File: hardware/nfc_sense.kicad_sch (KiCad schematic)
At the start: 27 parts, among them U1 TMP112AIDRLT, U2 RF430CL330HIRGTR‎, U3 ATtiny3227-M

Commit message: triangle extension
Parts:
- removed C8: 0.1 yF, Capacitor_SMD:C_0603_1608Metric, symbol Device:C
- removed D3: D_Schottky, Diode_SMD:D_0603_1608Metric_Pad1.05x0.95mm_HandSolder, symbol Device:D_Schottky
- removed R4: 10k, Resistor_SMD:R_0603_1608Metric_Pad0.98x0.95mm_HandSolder, symbol Device:R
- removed TP3, TP5: TestPoint, TestPoint:TestPoint_Pad_D1.0mm, symbol Connector:TestPoint

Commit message: attiny426 revision
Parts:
- removed U3: ATtiny3227-M, Package_DFN_QFN:QFN-24-1EP_4x4mm_P0.5mm_EP2.6x2.6mm, symbol MCU_Microchip_ATtiny:ATtiny3227-M
- added TP4: TestPoint, TestPoint:TestPoint_Pad_D1.0mm, symbol Connector:TestPoint
- added U3: ATtiny426-M, Package_DFN_QFN:VQFN-20-1EP_3x3mm_P0.4mm_EP1.7x1.7mm, symbol MCU_Microchip_ATtiny:ATtiny426-M
- renumbered TP4 to TP3
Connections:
- net ALERT: now also U3.18 (PC3)
- net GND: now also U3.21 (GND), U3.3 (GND)
- net RF430_INT: now also U3.10 (PB4)
- net RF430_RST: now also U3.9 (PB5)
- net RX: now also U3.11 (PB3)
- net SCL: now also U3.14 (PB0)
- net SDA: now also U3.13 (PB1)
- net TX: now also U3.12 (PB2)
- net UPDI: now also U3.19 (~{RESET}/PA0)
- net VCC: now also TP4.1, U3.4 (VCC)

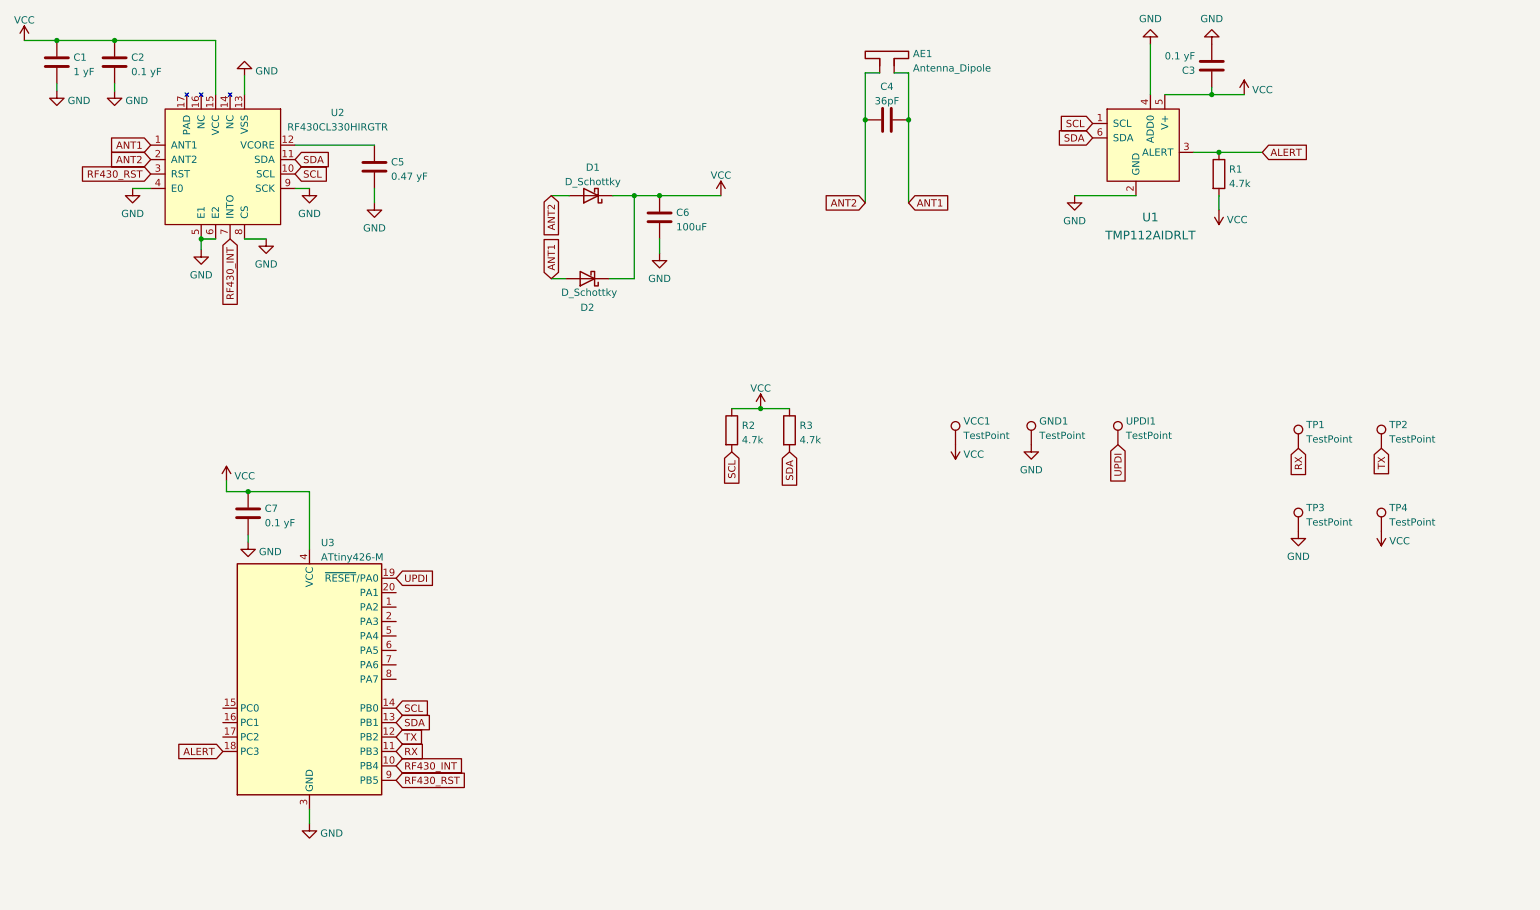
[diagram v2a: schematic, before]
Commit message: changed to attiny 1626
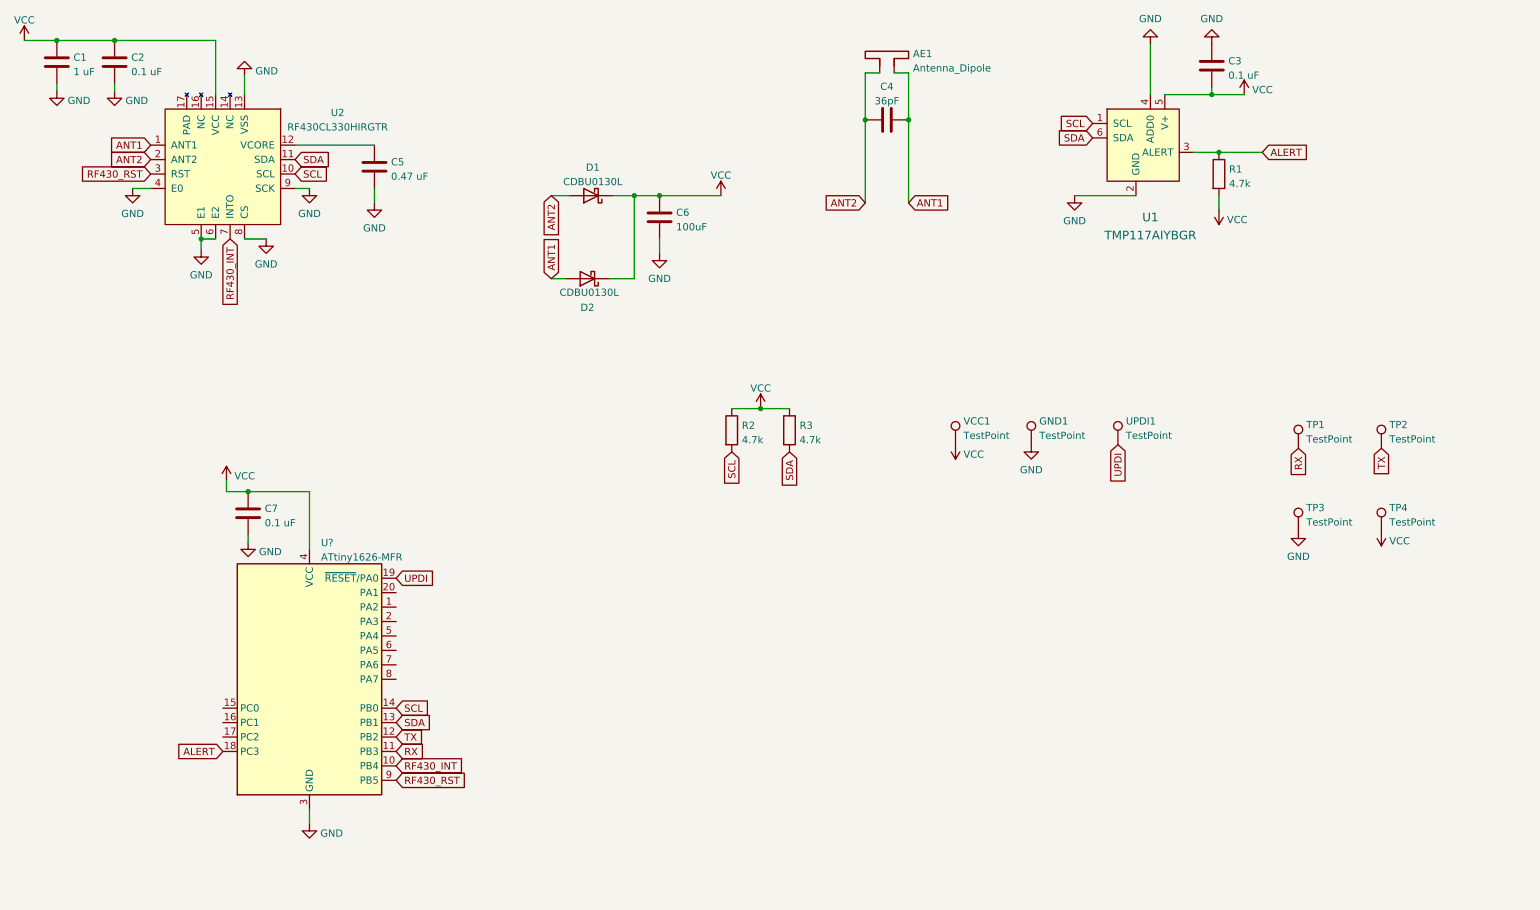
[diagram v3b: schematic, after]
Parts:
- removed U3: ATtiny426-M, Package_DFN_QFN:VQFN-20-1EP_3x3mm_P0.4mm_EP1.7x1.7mm, symbol MCU_Microchip_ATtiny:ATtiny426-M
- added U?: ATtiny1626-MFR, Package_DFN_QFN:VQFN-20-1EP_3x3mm_P0.4mm_EP1.7x1.7mm, symbol MCU_Microchip_ATtiny:ATtiny1626-M
- C1: value 1 yF -> 1 uF
- C2, C3, C7: value 0.1 yF -> 0.1 uF
- C5: value 0.47 yF -> 0.47 uF
- D1, D2: value D_Schottky -> CDBU0130L
- U1: value TMP112AIDRLT -> TMP117AIYBGR
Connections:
- net ALERT: now also U?.18 (PC3)
- net GND: now also U?.21 (GND), U?.3 (GND)
- net RF430_INT: now also U?.10 (PB4)
- net RF430_RST: now also U?.9 (PB5)
- net RX: now also U?.11 (PB3)
- net SCL: now also U?.14 (PB0)
- net SDA: now also U?.13 (PB1)
- net TX: now also U?.12 (PB2)
- net UPDI: now also U?.19 (~{RESET}/PA0)
- net VCC: now also U?.4 (VCC)

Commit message: individual case part cutouts
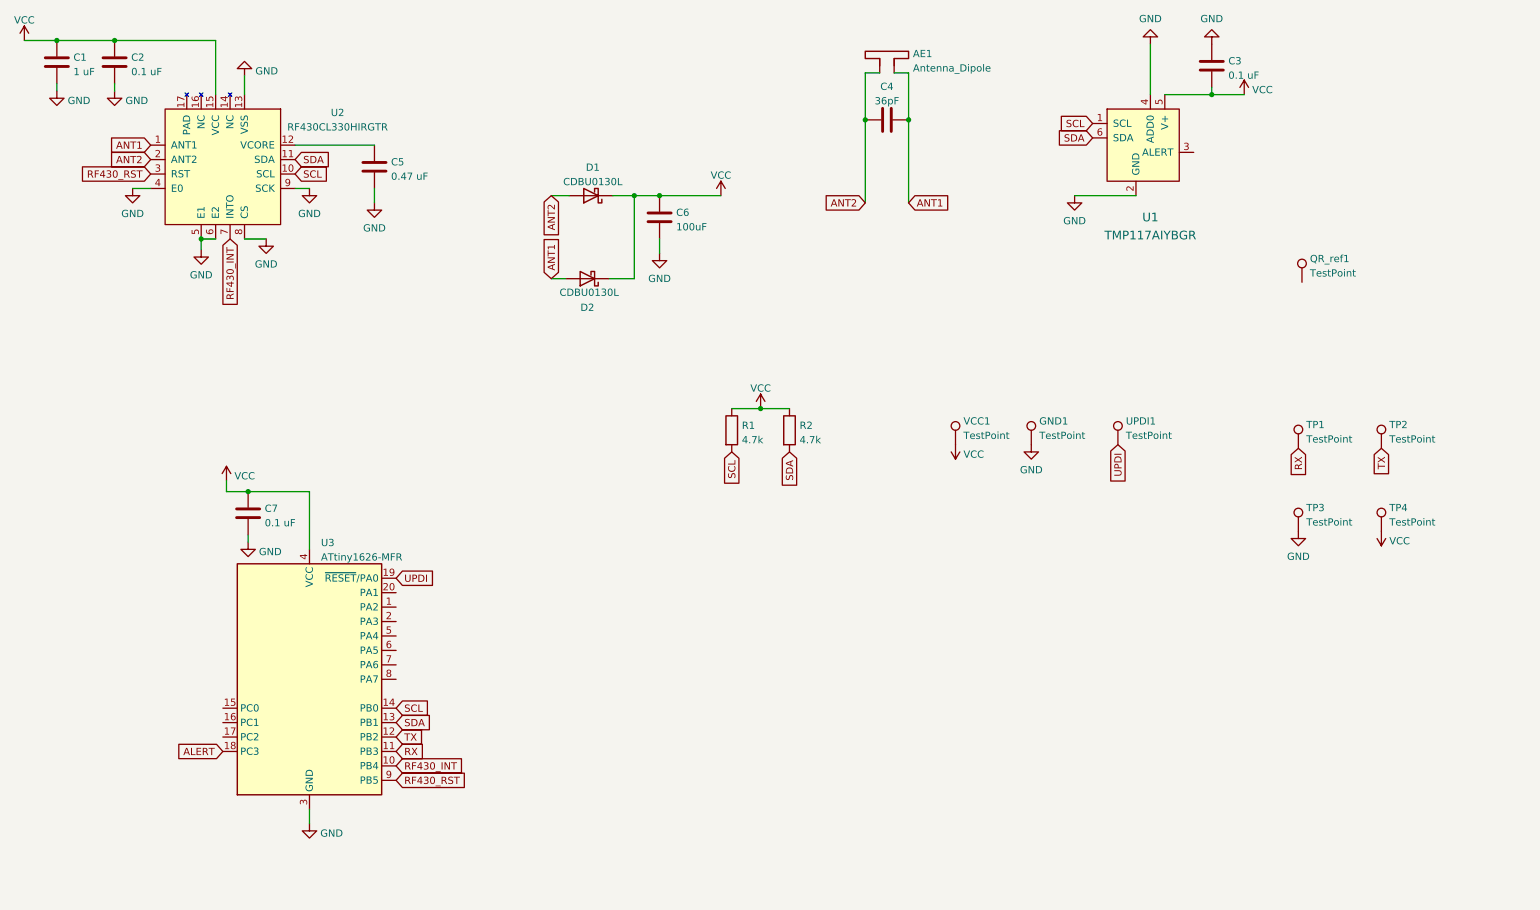
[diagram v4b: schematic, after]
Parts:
- removed R1: 4.7k, Resistor_SMD:R_0603_1608Metric_Pad0.98x0.95mm_HandSolder, symbol Device:R
- added QR_ref1: TestPoint, unsurv_offline_pcb_footprints:QR_shop, symbol Connector:TestPoint
- gave numbers to parts that had none: 1
- renumbered R2 to R1, R3 to R2
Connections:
- net ALERT: no longer U1.3 (ALERT)

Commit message: rev 2
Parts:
- added C7: 47uF, Capacitor_SMD:C_0603_1608Metric, symbol Device:C
- C6: value 100uF -> 47uF; footprint Capacitor_SMD:C_1206_3216Metric -> Capacitor_SMD:C_0603_1608Metric
- U1: value TMP117AIYBGR -> TMP117AIDRVR; footprint unsurv_offline_pcb_footprints:TMP117 -> unsurv_offline_pcb_footprints:TMP117 WSON-6-1EP_2x2mm_P0.65mm
- renumbered C7 to C8
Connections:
- net GND: now also C7.2
- net VCC: now also C7.1
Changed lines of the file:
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@@
   (junction (at 30.48 19.05) (diameter 0) (color 0 0 0 0)
   )
+  (junction (at 138.43 46.355) (diameter 0) (color 0 0 0 0)
+  )
   (wire (pts (xy 20.32 26.67) (xy 20.32 27.94))
     (stroke (width 0) (type default) (color 0 0 0 0))
@@
     (stroke (width 0) (type default) (color 0 0 0 0))
   )
+  (wire (pts (xy 138.43 53.975) (xy 138.43 56.515))
+    (stroke (width 0) (type default) (color 0 0 0 0))
+  )
   (wire (pts (xy 53.34 25.273) (xy 53.34 28.575))
     (stroke (width 0) (type default) (color 0 0 0 0))
@@
     (stroke (width 0) (type default) (color 0 0 0 0))
   )
-  (wire (pts (xy 126.365 46.355) (xy 137.16 46.355))
+  (wire (pts (xy 126.365 46.355) (xy 138.43 46.355))
+    (stroke (width 0) (type default) (color 0 0 0 0))
+  )
+  (wire (pts (xy 138.43 46.355) (xy 145.415 46.355))
     (stroke (width 0) (type default) (color 0 0 0 0))
   )
@@
   (symbol (lib_id "power:VCC") (at 253.365 105.41 180) (unit 1)
     (in_bom yes) (on_board yes) (fields_autoplaced)
-    (property "Reference" "#PWR021" (id 0) (at 253.365 101.6 0)
+    (property "Reference" "#PWR022" (id 0) (at 253.365 101.6 0)
       (effects (font (size 1.27 1.27)) hide)
     )
@@
       (effects (font (size 1.27 1.27)) (justify left))
     )
-    (property "Value" "100uF" (id 1) (at 129.286 51.8672 0)
-      (effects (font (size 1.27 1.27)) (justify left))
-    )
-    (property "Footprint" "Capacitor_SMD:C_1206_3216Metric" (id 2) (at 127.3302 53.975 0)
+    (property "Value" "47uF" (id 1) (at 129.286 51.8672 0)
+      (effects (font (size 1.27 1.27)) (justify left))
+    )
+    (property "Footprint" "Capacitor_SMD:C_0603_1608Metric" (id 2) (at 127.3302 53.975 0)
       (effects (font (size 1.27 1.27)) hide)
     )
@@
   (symbol (lib_id "power:GND") (at 191.77 90.17 0) (unit 1)
     (in_bom yes) (on_board yes) (fields_autoplaced)
-    (property "Reference" "#PWR018" (id 0) (at 191.77 96.52 0)
+    (property "Reference" "#PWR019" (id 0) (at 191.77 96.52 0)
       (effects (font (size 1.27 1.27)) hide)
     )
@@
     (pin "2")
   )
-  (symbol (lib_id "power:VCC") (at 137.16 46.355 0) (unit 1)
-    (in_bom yes) (on_board yes) (fields_autoplaced)
-    (property "Reference" "#PWR010" (id 0) (at 137.16 50.165 0)
-      (effects (font (size 1.27 1.27)) hide)
-    )
-    (property "Value" "VCC" (id 1) (at 137.16 42.7792 0))
-    (property "Footprint" "" (id 2) (at 137.16 46.355 0)
-      (effects (font (size 1.27 1.27)) hide)
-    )
-    (property "Datasheet" "" (id 3) (at 137.16 46.355 0)
+  (symbol (lib_id "power:VCC") (at 145.415 46.355 0) (unit 1)
+    (in_bom yes) (on_board yes) (fields_autoplaced)
+    (property "Reference" "#PWR010" (id 0) (at 145.415 50.165 0)
+      (effects (font (size 1.27 1.27)) hide)
+    )
+    (property "Value" "VCC" (id 1) (at 145.415 42.7792 0))
+    (property "Footprint" "" (id 2) (at 145.415 46.355 0)
+      (effects (font (size 1.27 1.27)) hide)
+    )
+    (property "Datasheet" "" (id 3) (at 145.415 46.355 0)
       (effects (font (size 1.27 1.27)) hide)
     )
@@
       (effects (font (size 1.524 1.524)))
     )
-    (property "Value" "TMP117AIYBGR" (id 1) (at 212.725 53.34 0)
+    (property "Value" "TMP117AIDRVR" (id 1) (at 212.725 53.34 0)
       (effects (font (size 1.524 1.524)))
     )
-    (property "Footprint" "unsurv_offline_pcb_footprints:TMP117" (id 2) (at 217.805 33.655 0)
+    (property "Footprint" "unsurv_offline_pcb_footprints:TMP117 WSON-6-1EP_2x2mm_P0.65mm" (id 2) (at 217.805 33.655 0)
       (effects (font (size 1.524 1.524)) (justify left) hide)
     )
@@
   (symbol (lib_id "power:VCC") (at 144.145 83.82 0) (unit 1)
     (in_bom yes) (on_board yes) (fields_autoplaced)
-    (property "Reference" "#PWR016" (id 0) (at 144.145 87.63 0)
+    (property "Reference" "#PWR017" (id 0) (at 144.145 87.63 0)
       (effects (font (size 1.27 1.27)) hide)
     )
@@
   (symbol (lib_id "Device:C") (at 53.975 102.235 0) (unit 1)
     (in_bom yes) (on_board yes) (fields_autoplaced)
-    (property "Reference" "C7" (id 0) (at 56.896 101.4003 0)
+    (property "Reference" "C8" (id 0) (at 56.896 101.4003 0)
       (effects (font (size 1.27 1.27)) (justify left))
     )
@@
     (pin "1")
   )
+  (symbol (lib_id "power:GND") (at 138.43 56.515 0) (unit 1)
+    (in_bom yes) (on_board yes) (fields_autoplaced)
+    (property "Reference" "#PWR016" (id 0) (at 138.43 62.865 0)
+      (effects (font (size 1.27 1.27)) hide)
+    )
+    (property "Value" "GND" (id 1) (at 138.43 60.9584 0))
+    (property "Footprint" "" (id 2) (at 138.43 56.515 0)
+      (effects (font (size 1.27 1.27)) hide)
+    )
+    (property "Datasheet" "" (id 3) (at 138.43 56.515 0)
+      (effects (font (size 1.27 1.27)) hide)
+    )
+    (pin "1")
+  )
   (symbol (lib_id "power:VCC") (at 178.435 90.17 180) (unit 1)
     (in_bom yes) (on_board yes) (fields_autoplaced)
-    (property "Reference" "#PWR017" (id 0) (at 178.435 86.36 0)
+    (property "Reference" "#PWR018" (id 0) (at 178.435 86.36 0)
       (effects (font (size 1.27 1.27)) hide)
     )
@@
   (symbol (lib_id "power:GND") (at 238.76 105.41 0) (unit 1)
     (in_bom yes) (on_board yes) (fields_autoplaced)
-    (property "Reference" "#PWR020" (id 0) (at 238.76 111.76 0)
+    (property "Reference" "#PWR021" (id 0) (at 238.76 111.76 0)
       (effects (font (size 1.27 1.27)) hide)
     )
@@
   (symbol (lib_id "power:GND") (at 64.77 156.845 0) (unit 1)
     (in_bom yes) (on_board yes) (fields_autoplaced)
-    (property "Reference" "#PWR023" (id 0) (at 64.77 163.195 0)
+    (property "Reference" "#PWR024" (id 0) (at 64.77 163.195 0)
       (effects (font (size 1.27 1.27)) hide)
     )
@@
     (pin "1")
   )
+  (symbol (lib_id "Device:C") (at 138.43 50.165 0) (unit 1)
+    (in_bom yes) (on_board yes) (fields_autoplaced)
+    (property "Reference" "C7" (id 0) (at 141.351 49.3303 0)
+      (effects (font (size 1.27 1.27)) (justify left))
+    )
+    (property "Value" "47uF" (id 1) (at 141.351 51.8672 0)
+      (effects (font (size 1.27 1.27)) (justify left))
+    )
+    (property "Footprint" "Capacitor_SMD:C_0603_1608Metric" (id 2) (at 139.3952 53.975 0)
+      (effects (font (size 1.27 1.27)) hide)
+    )
+    (property "Datasheet" "~" (id 3) (at 138.43 50.165 0)
+      (effects (font (size 1.27 1.27)) hide)
+    )
+    (pin "1")
+    (pin "2")
+  )
   (symbol (lib_id "power:GND") (at 30.48 27.94 0) (unit 1)
     (in_bom yes) (on_board yes) (fields_autoplaced)
@@
   (symbol (lib_id "power:GND") (at 53.975 107.315 0) (unit 1)
     (in_bom yes) (on_board yes) (fields_autoplaced)
-    (property "Reference" "#PWR022" (id 0) (at 53.975 113.665 0)
+    (property "Reference" "#PWR023" (id 0) (at 53.975 113.665 0)
       (effects (font (size 1.27 1.27)) hide)
     )
@@
   (symbol (lib_id "power:VCC") (at 50.165 96.52 0) (unit 1)
     (in_bom yes) (on_board yes) (fields_autoplaced)
-    (property "Reference" "#PWR019" (id 0) (at 50.165 100.33 0)
+    (property "Reference" "#PWR020" (id 0) (at 50.165 100.33 0)
       (effects (font (size 1.27 1.27)) hide)
     )
@@
       (reference "#PWR015") (unit 1) (value "GND") (footprint "")
     )
+    (path "/bb268d58-5251-4bc1-8150-e36988c3bcc5"
+      (reference "#PWR016") (unit 1) (value "GND") (footprint "")
+    )
     (path "/6d49dad5-ea06-4d39-9984-0212ae848129"
-      (reference "#PWR016") (unit 1) (value "VCC") (footprint "")
+      (reference "#PWR017") (unit 1) (value "VCC") (footprint "")
     )
     (path "/c1f5a60a-b153-4fa9-8914-58486ad5ba0d"
-      (reference "#PWR017") (unit 1) (value "VCC") (footprint "")
+      (reference "#PWR018") (unit 1) (value "VCC") (footprint "")
     )
     (path "/487928cd-2468-418e-8511-756b5d71e0db"
-      (reference "#PWR018") (unit 1) (value "GND") (footprint "")
+      (reference "#PWR019") (unit 1) (value "GND") (footprint "")
     )
     (path "/fbb2136a-66da-49ac-ba3d-ab2ef660bc11"
-      (reference "#PWR019") (unit 1) (value "VCC") (footprint "")
+      (reference "#PWR020") (unit 1) (value "VCC") (footprint "")
     )
     (path "/c7ccfdba-c341-451c-8972-b9b82c4a5437"
-      (reference "#PWR020") (unit 1) (value "GND") (footprint "")
+      (reference "#PWR021") (unit 1) (value "GND") (footprint "")
     )
     (path "/32280050-40a1-4f78-98fd-96fb75da1eff"
-      (reference "#PWR021") (unit 1) (value "VCC") (footprint "")
+      (reference "#PWR022") (unit 1) (value "VCC") (footprint "")
     )
     (path "/f4ca3cad-c229-4741-81cb-dbd46bf2aec0"
-      (reference "#PWR022") (unit 1) (value "GND") (footprint "")
+      (reference "#PWR023") (unit 1) (value "GND") (footprint "")
     )
     (path "/daf5f378-bf82-4372-99dc-961719301258"
-      (reference "#PWR023") (unit 1) (value "GND") (footprint "")
+      (reference "#PWR024") (unit 1) (value "GND") (footprint "")
     )
     (path "/c62370cb-5769-450d-8ea9-f65c15d69aea"
@@
     )
     (path "/3cca1b81-edf2-4dd5-864e-c8a1ba6c7441"
-      (reference "C6") (unit 1) (value "100uF") (footprint "Capacitor_SMD:C_1206_3216Metric")
+      (reference "C6") (unit 1) (value "47uF") (footprint "Capacitor_SMD:C_0603_1608Metric")
+    )
+    (path "/dd49231d-c829-45bb-aa59-e259aca61903"
+      (reference "C7") (unit 1) (value "47uF") (footprint "Capacitor_SMD:C_0603_1608Metric")
     )
     (path "/a40e5e21-9a36-4f52-a95f-9b6b82195ce1"
-      (reference "C7") (unit 1) (value "0.1 uF") (footprint "Capacitor_SMD:C_0603_1608Metric")
+      (reference "C8") (unit 1) (value "0.1 uF") (footprint "Capacitor_SMD:C_0603_1608Metric")
     )
     (path "/39d138d9-0013-4c64-a1ed-8ebc0d7ee611"
@@
     )
     (path "/66c5039d-30d6-403e-9b61-a8f7c5bee423"
-      (reference "U1") (unit 1) (value "TMP117AIYBGR") (footprint "unsurv_offline_pcb_footprints:TMP117")
+      (reference "U1") (unit 1) (value "TMP117AIDRVR") (footprint "unsurv_offline_pcb_footprints:TMP117 WSON-6-1EP_2x2mm_P0.65mm")
     )
     (path "/2573d7f5-93df-4b04-86ca-b100ed4156d5"

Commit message: kicad 8 + panelization
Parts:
- U1: MPN TMP112AIDRLT -> TMP117AIDRVR
